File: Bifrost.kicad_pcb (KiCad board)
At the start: 4 copper layers, 68.6 x 53.3 mm, 69 parts, among them J1 OIP, J2 Conn_01x03_Male, J3 Conn_01x03_Male, U2 AD5932, U3 LMH6881, U5 AD5932, X1 SPXO-50M

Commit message: v1.0 of the routing
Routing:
- net /IO2: track 0.00 -> 62.2 mm, vias 0 -> 1
- net /IO3: track 0.00 -> 59.7 mm, vias 0 -> 1
- net /IO7: track 0.00 -> 44.3 mm
- net /IO5: track 0.00 -> 42.7 mm, vias 0 -> 2
- net /SEN3: track 0.00 -> 41.2 mm, vias 0 -> 1
- net /IO6: track 0.00 -> 39.9 mm, vias 0 -> 2
- net /IO4: track 0.00 -> 37.9 mm
- net /SEN: track 0.00 -> 37.1 mm, vias 0 -> 2
- net /SDI: track 25.8 -> 58.0 mm, vias 1 -> 3
- net /SEN2: track 0.00 -> 28.4 mm
- net /SCK: track 37.6 -> 51.0 mm, vias 0 -> 1
- net Net-(J2-Pad2): track 0.00 -> 5.04 mm
- net VCC: track 10.1 -> 10.4 mm, vias 9 -> 10

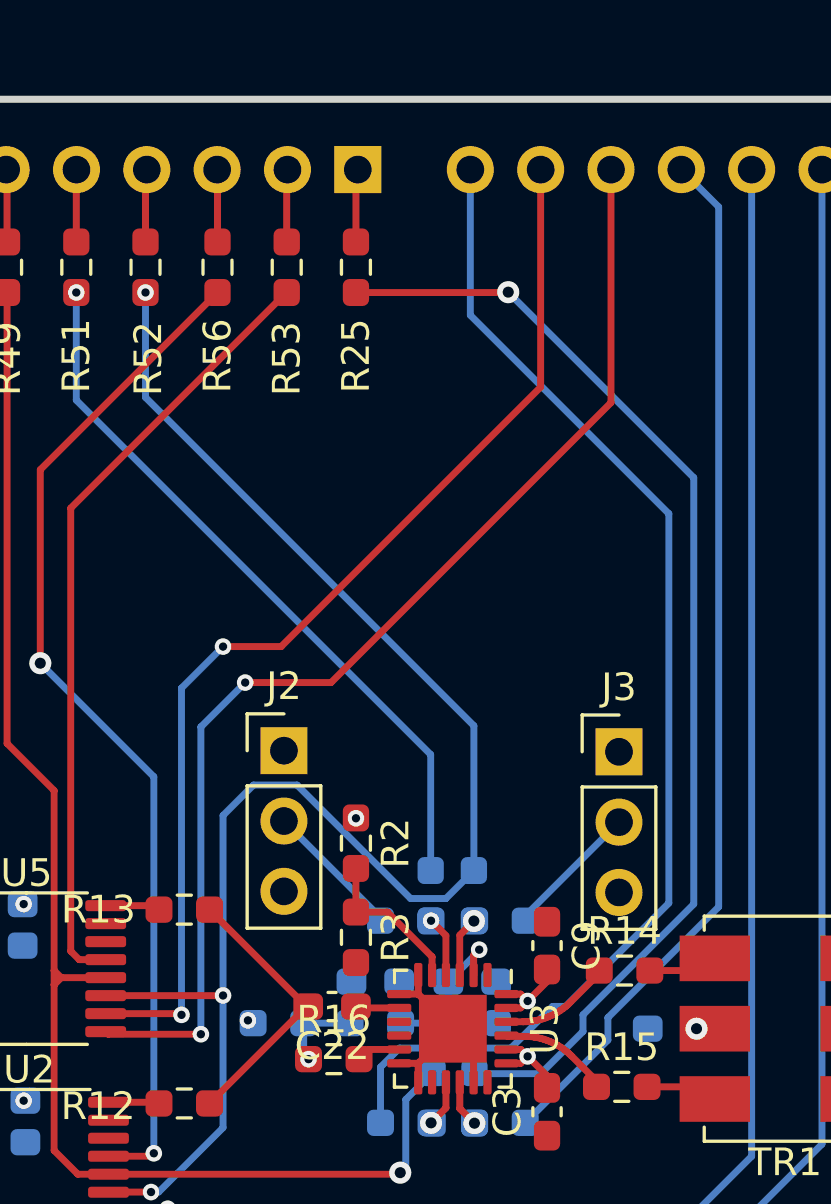
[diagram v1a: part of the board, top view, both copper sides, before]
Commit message: Position des jumper/switch
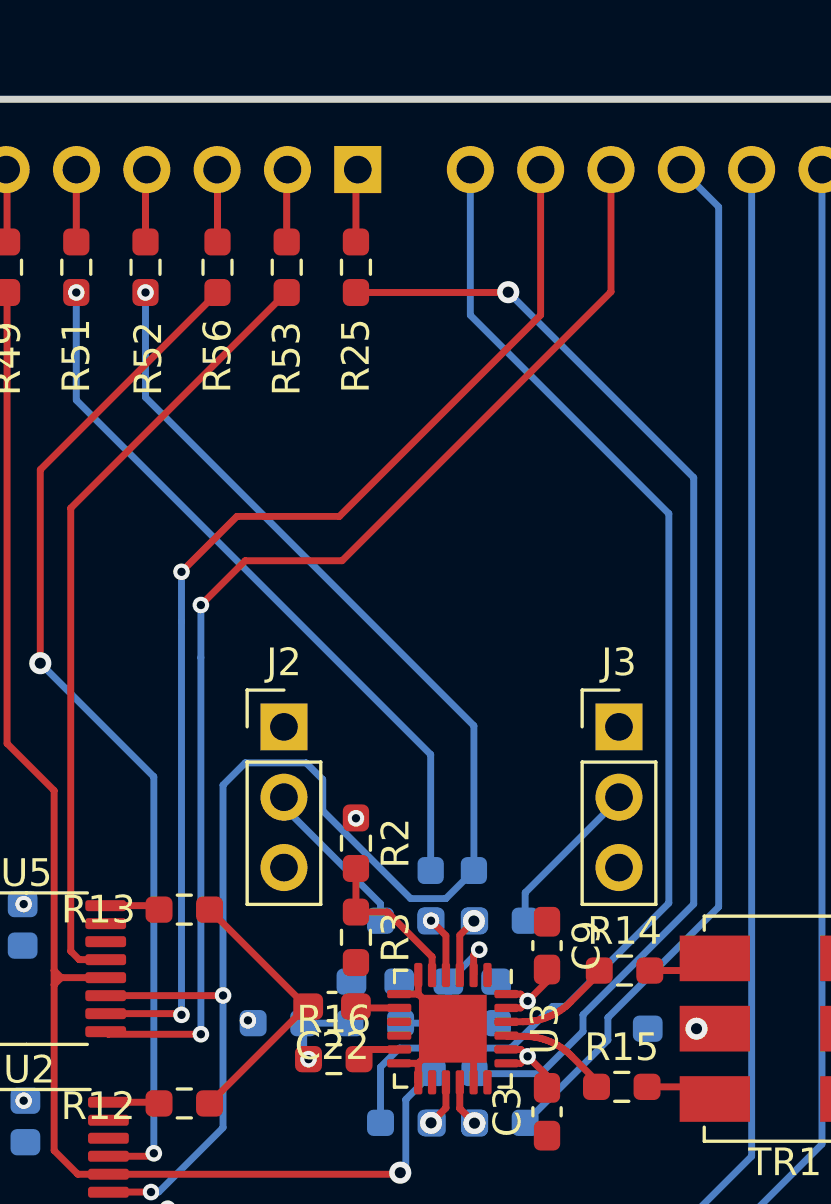
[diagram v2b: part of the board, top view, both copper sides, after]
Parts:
- moved J3 0.90 mm to (165.3, 101.0)
- moved J2 0.86 mm to (153.2, 101.0)
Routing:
- net /SDI: track 58.0 -> 60.0 mm
- net /IO6: track 39.9 -> 40.8 mm
- net Net-(J3-Pad2): track 4.96 -> 5.86 mm
- net Net-(J2-Pad2): track 5.04 -> 5.90 mm

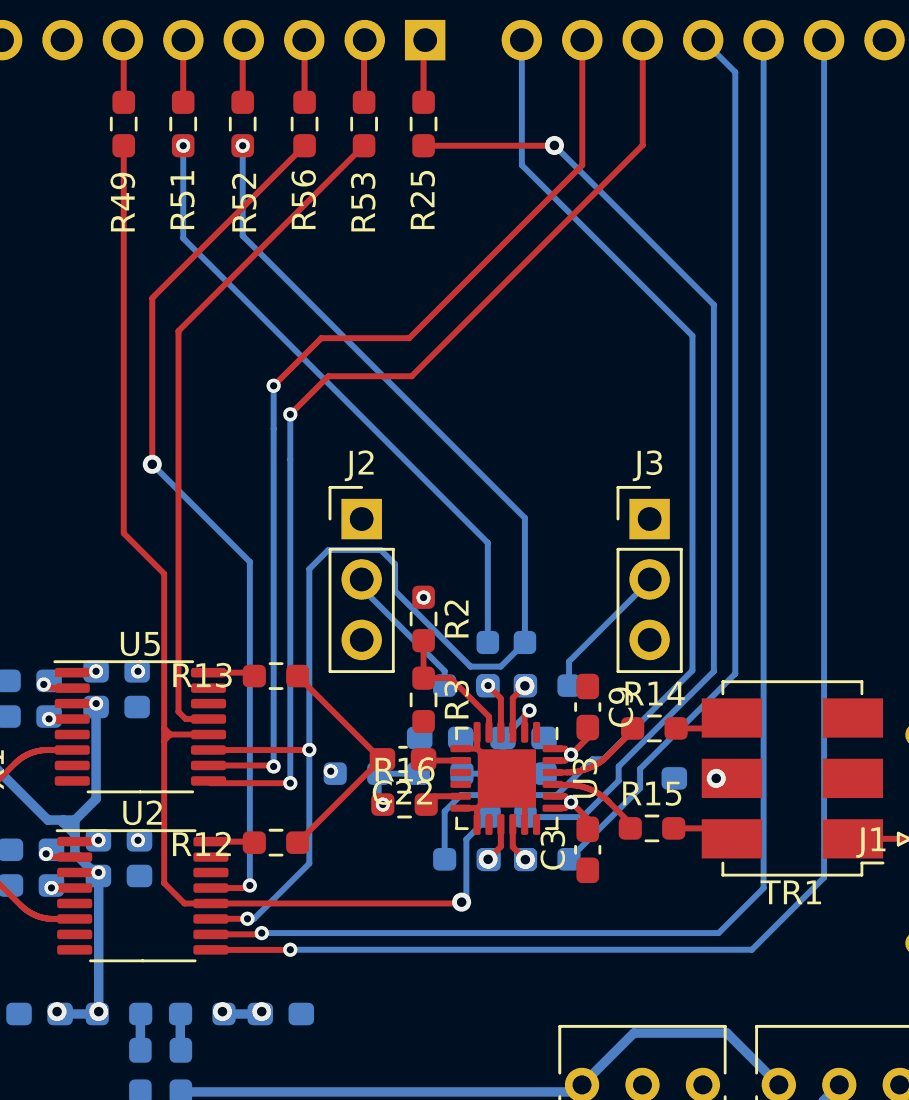
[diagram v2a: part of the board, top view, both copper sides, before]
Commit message: Optimized routing
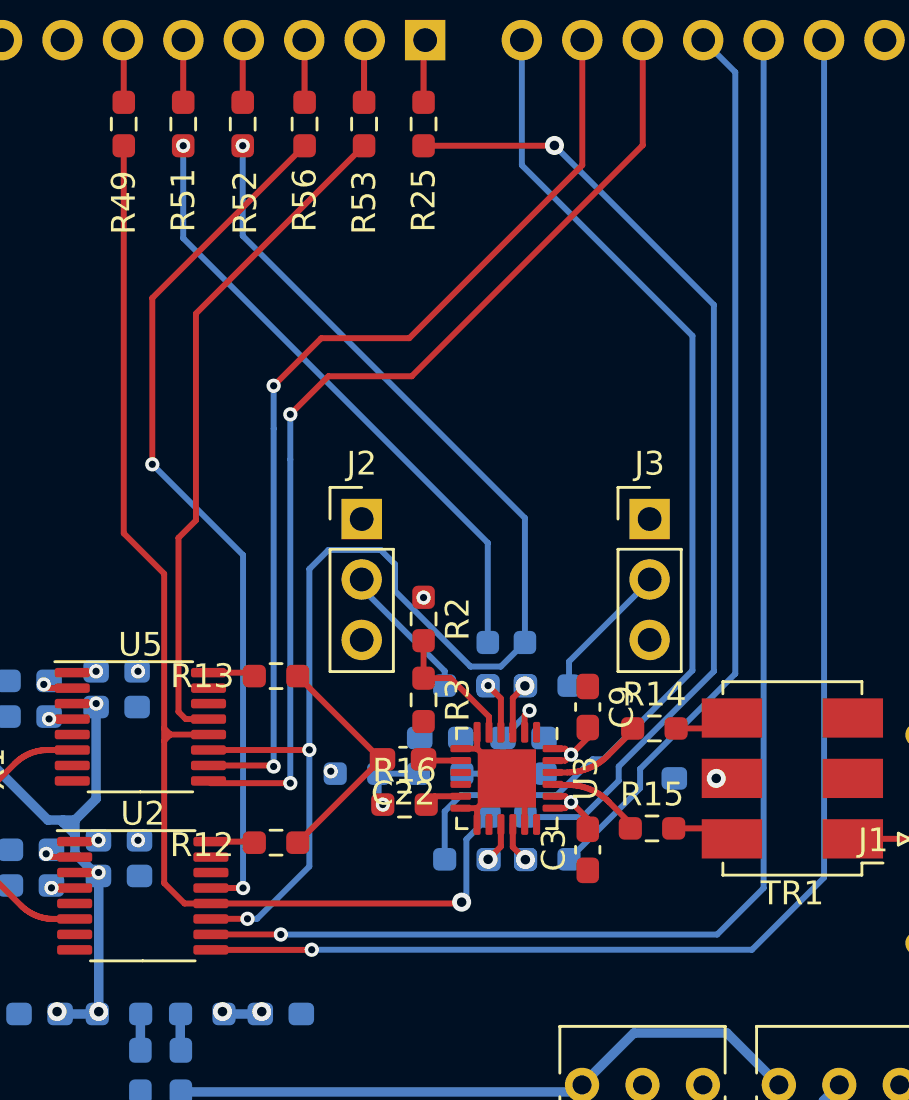
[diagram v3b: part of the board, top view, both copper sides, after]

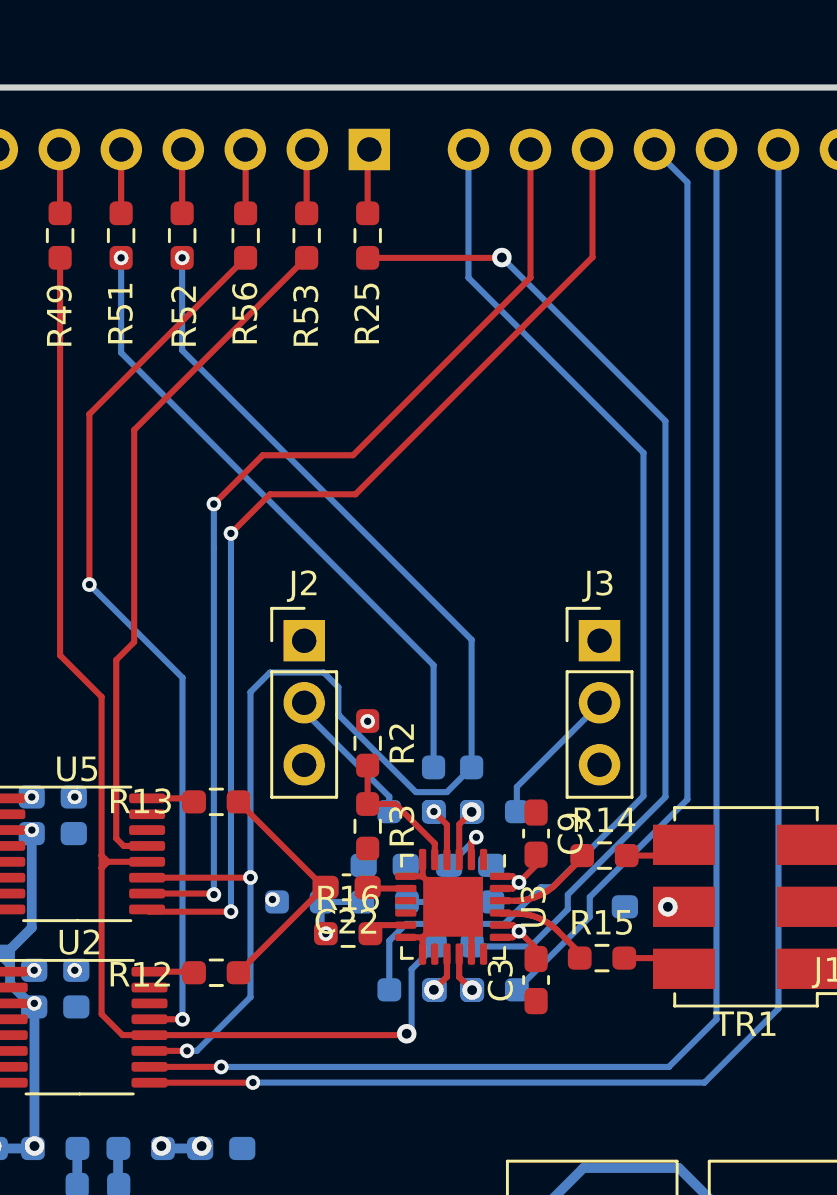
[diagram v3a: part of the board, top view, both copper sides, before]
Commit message: Added thermal vias for the LMH6881 and re-routed to accommodate
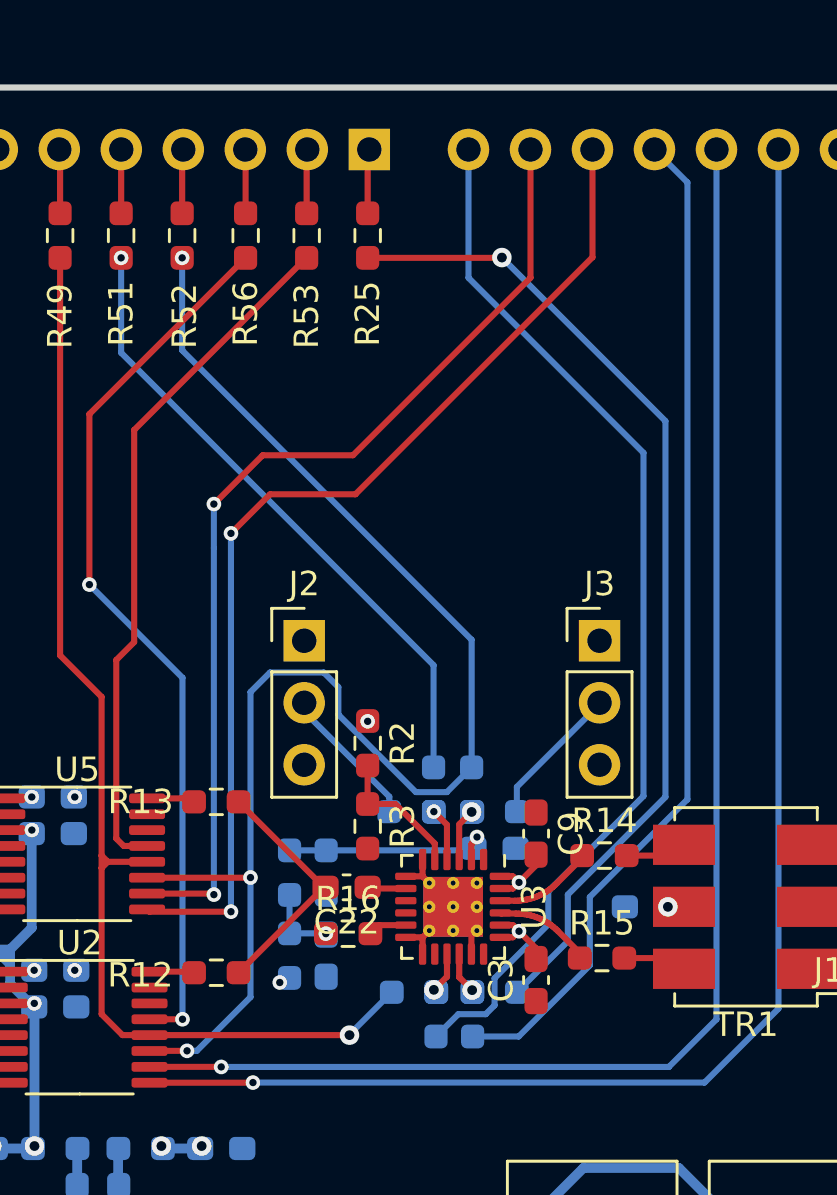
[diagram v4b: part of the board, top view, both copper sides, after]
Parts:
- L1, L2: value 10u -> 1u
- R10, R11: value 2 -> 0.2
- U3: footprint Package_DFN_QFN:WQFN-24-1EP_4x4mm_P0.5mm_EP2.45x2.45mm -> Package_DFN_QFN:WQFN-24-1EP_4x4mm_P0.5mm_EP2.45x2.45mm_ThermalVias
- moved R5 6.02 mm to (154.1, 110.5), turned to 270 degrees
- moved C24 4.41 mm to (154.1, 113.9), turned to 90 degrees
- moved R1 4.08 mm to (152.6, 110.5), turned to 90 degrees
- moved R4 2.24 mm to (152.6, 113.9), turned to 270 degrees
- moved R22 1.41 mm to (158.6, 116.3), turned to 270 degrees
- moved R23 1.36 mm to (161.0, 115.4), turned to 0 degrees
- moved R24 1.35 mm to (160.1, 116.3), turned to 270 degrees
- moved R21 1.33 mm to (157.7, 115.4), turned to 180 degrees
- moved C25 1.22 mm to (161.0, 109.5)
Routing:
- net /SCK: track 51.0 -> 47.0 mm
- net /IO4: track 37.9 -> 41.6 mm
- net /1.25V: track 5.81 -> 9.47 mm
- net /2.5V: track 4.57 -> 3.07 mm
- net /IO7: track 44.3 -> 43.5 mm

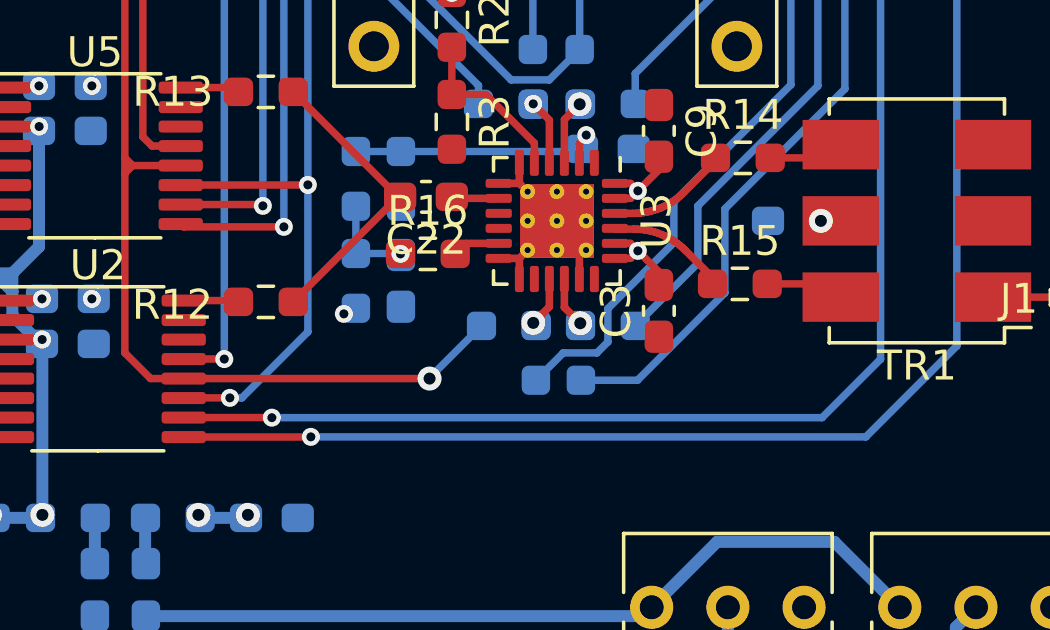
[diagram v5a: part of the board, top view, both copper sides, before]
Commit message: Bifrost_v2.0 launched to fab Modified LMH6881's thermal vias Rotated GND pads to better propagate GND
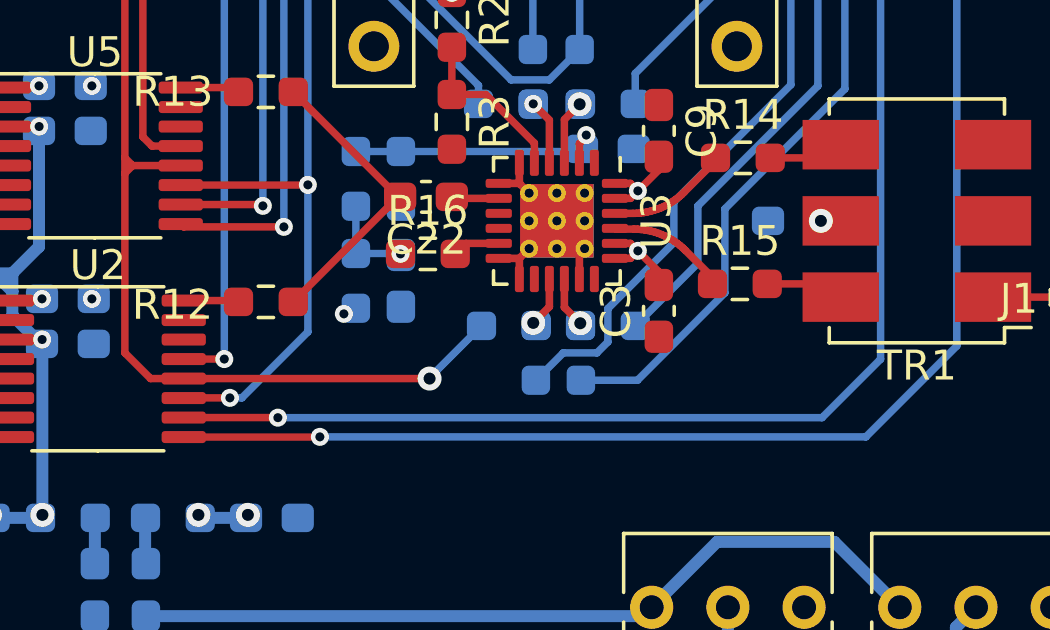
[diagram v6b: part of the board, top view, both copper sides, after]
